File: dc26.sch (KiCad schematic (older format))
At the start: 50 parts, among them J1 CONN_01X10, J2 CONN_01X10, J3 CONN_01X10, Y1 Crystal

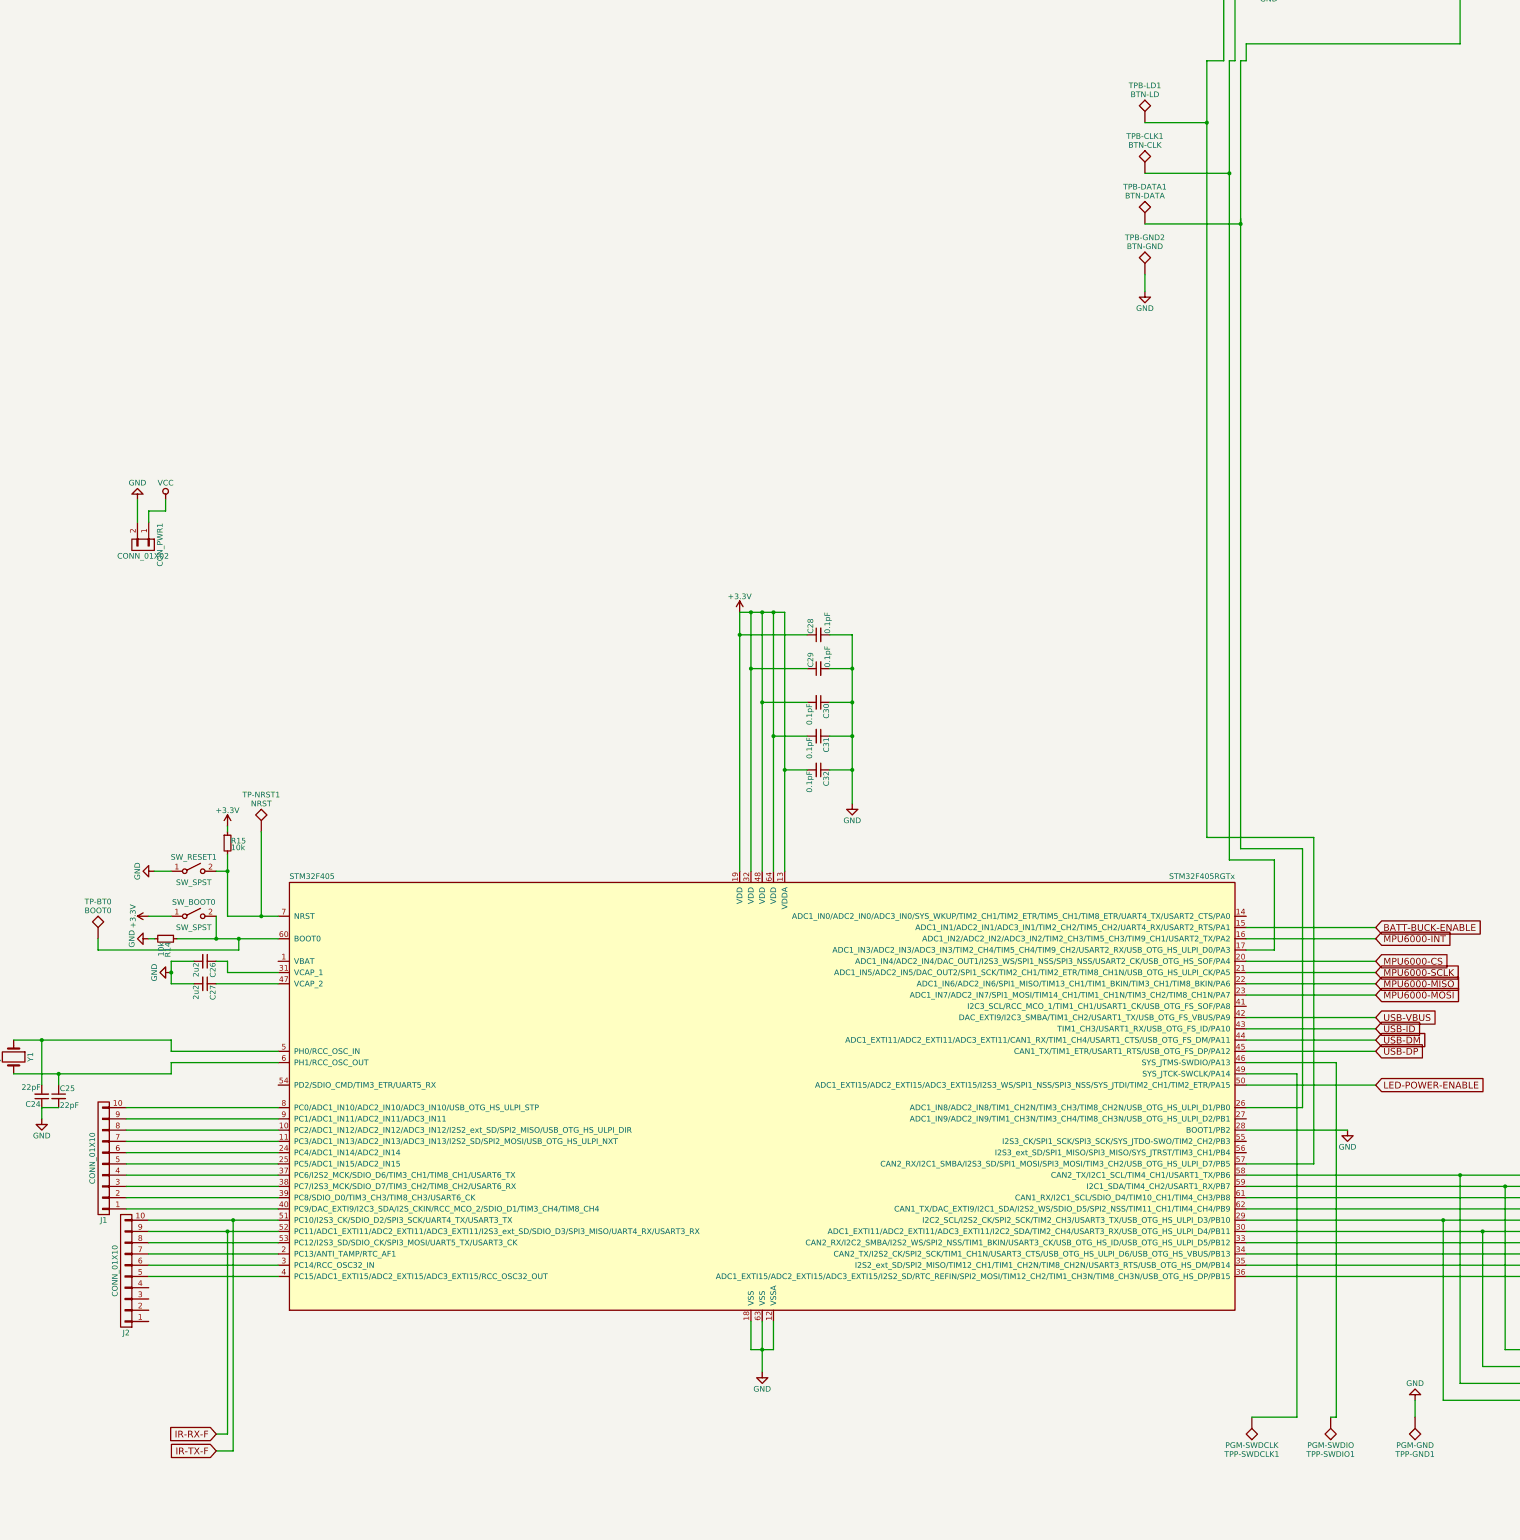
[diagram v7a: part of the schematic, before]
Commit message: Name changes on silk
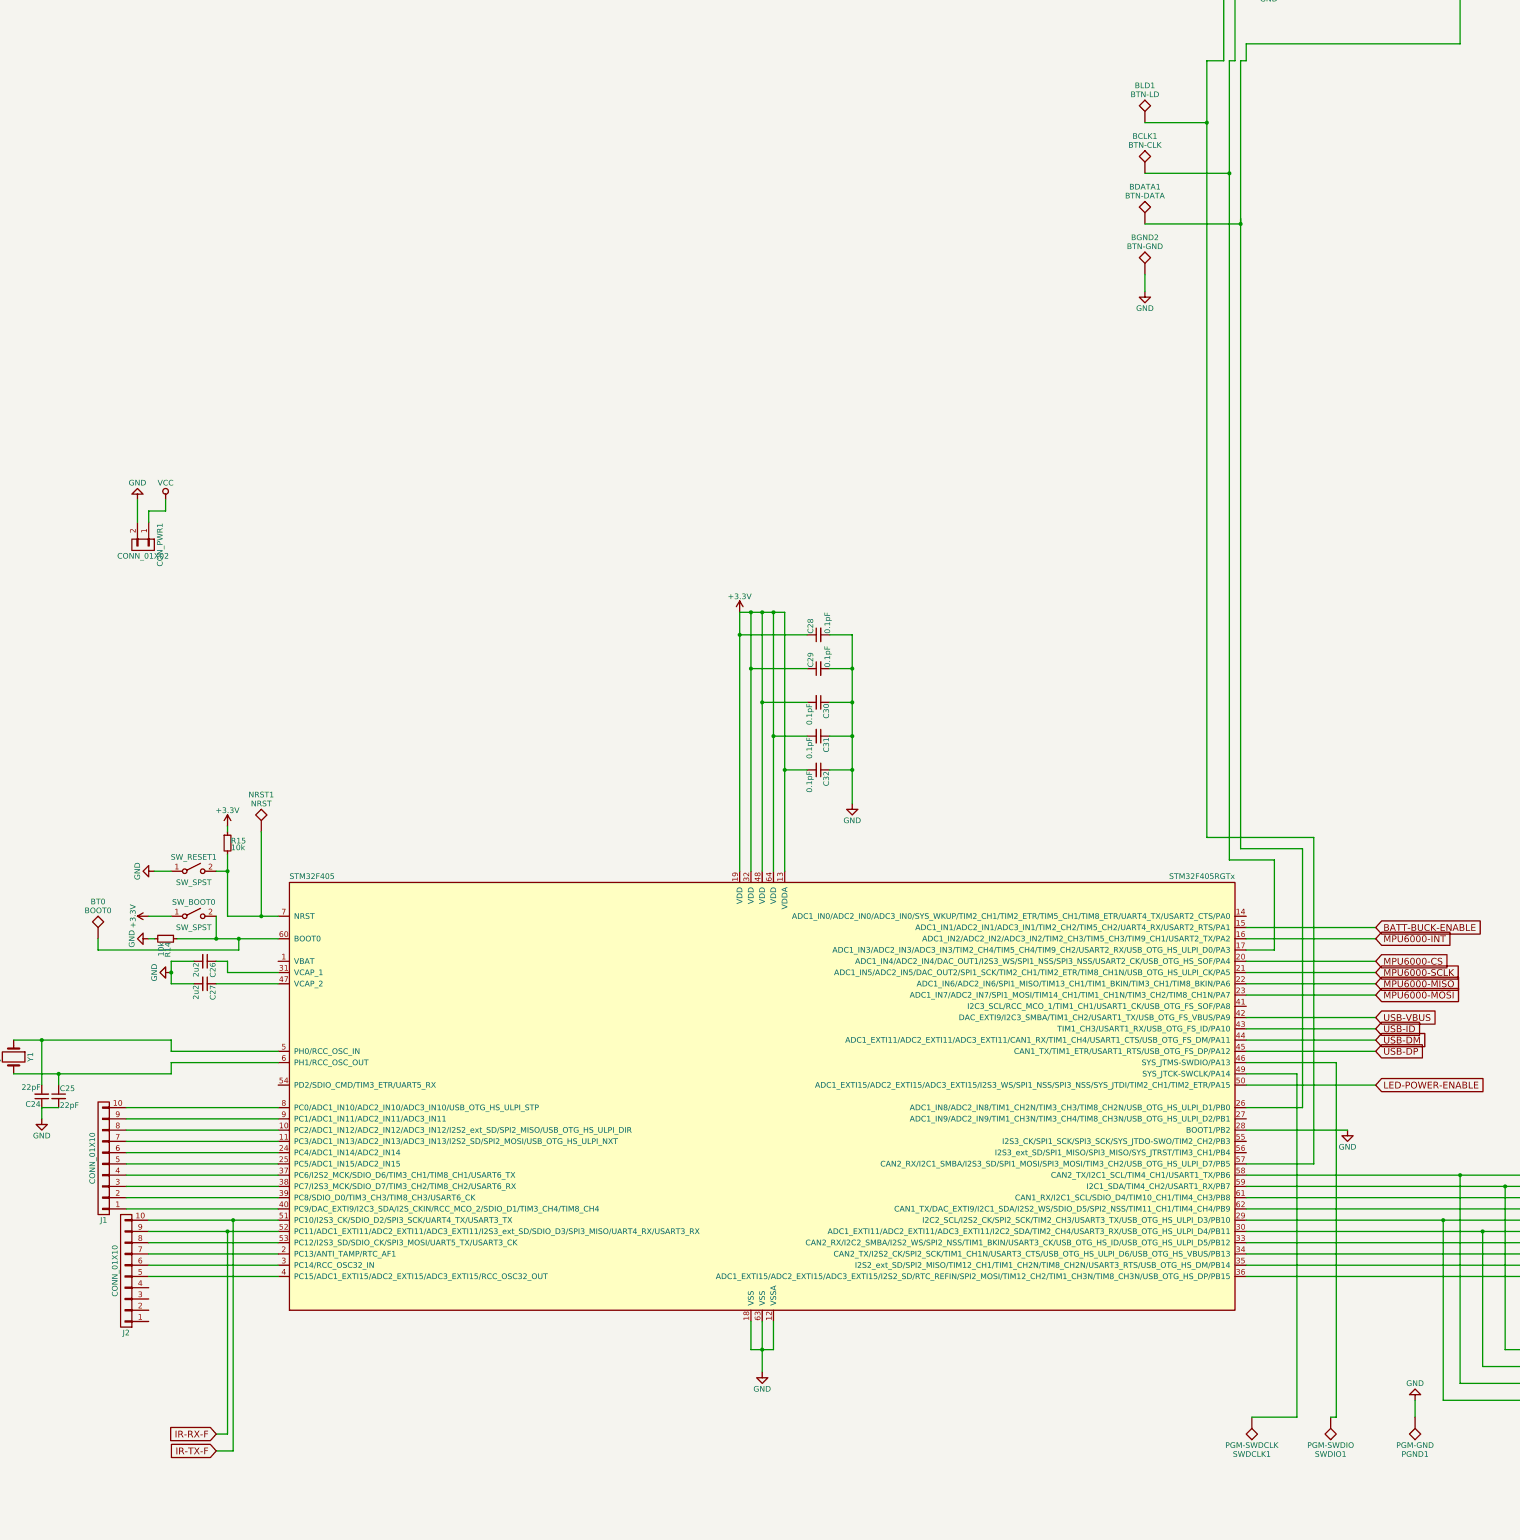
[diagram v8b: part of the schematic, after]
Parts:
- renumbered TPB-CLK1 to BCLK1, TPB-DATA1 to BDATA1, TPB-GND2 to BGND2, TPB-LD1 to BLD1, TP-BT0 to BT0, TP-NRST1 to NRST1, TPP-GND1 to PGND1, TPP-SWDCLK1 to SWDCLK1, TPP-SWDIO1 to SWDIO1
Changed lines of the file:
@@
 $EndComp
 $Comp
-L GND #PWR14
+L GND #PWR01
 U 1 1 5AD27FBE
 P -3450 -6450
-F 0 "#PWR14" H -3450 -6700 50  0001 C CNN
+F 0 "#PWR01" H -3450 -6700 50  0001 C CNN
 F 1 "GND" H -3450 -6600 50  0000 C CNN
 F 2 "" H -3450 -6450 50  0001 C CNN
@@
 $EndComp
 $Comp
-L GND #PWR2
+L GND #PWR02
 U 1 1 5AD5BD83
 P -12550 1050
-F 0 "#PWR2" H -12550 800 50  0001 C CNN
+F 0 "#PWR02" H -12550 800 50  0001 C CNN
 F 1 "GND" H -12550 900 50  0000 C CNN
 F 2 "" H -12550 1050 50  0001 C CNN
@@
 $EndComp
 $Comp
-L VCC #PWR6
+L VCC #PWR03
 U 1 1 5AD5C4E4
 P -12300 1050
-F 0 "#PWR6" H -12300 900 50  0001 C CNN
+F 0 "#PWR03" H -12300 900 50  0001 C CNN
 F 1 "VCC" H -12300 1200 50  0000 C CNN
 F 2 "" H -12300 1050 50  0001 C CNN
@@
 $EndComp
 $Comp
-L GND #PWR15
+L GND #PWR04
 U 1 1 5AD6E593
 P -2500 -5100
-F 0 "#PWR15" H -2500 -5350 50  0001 C CNN
+F 0 "#PWR04" H -2500 -5350 50  0001 C CNN
 F 1 "GND" H -2500 -5250 50  0000 C CNN
 F 2 "" H -2500 -5100 50  0001 C CNN
@@
 $EndComp
 $Comp
-L GND #PWR16
+L GND #PWR05
 U 1 1 5AD6F999
 P -2500 -3550
-F 0 "#PWR16" H -2500 -3800 50  0001 C CNN
+F 0 "#PWR05" H -2500 -3800 50  0001 C CNN
 F 1 "GND" H -2500 -3700 50  0000 C CNN
 F 2 "" H -2500 -3550 50  0001 C CNN
@@
 $EndComp
 $Comp
-L GND #PWR13
+L GND #PWR06
 U 1 1 5AD77A72
 P -3600 -800
-F 0 "#PWR13" H -3600 -1050 50  0001 C CNN
+F 0 "#PWR06" H -3600 -1050 50  0001 C CNN
 F 1 "GND" H -3600 -950 50  0000 C CNN
 F 2 "" H -3600 -800 50  0001 C CNN
@@
 $EndComp
 $Comp
-L GND #PWR10
+L GND #PWR07
 U 1 1 5B04F2A2
 P -7000 8800
-F 0 "#PWR10" H -7000 8550 50  0001 C CNN
+F 0 "#PWR07" H -7000 8550 50  0001 C CNN
 F 1 "GND" H -7000 8650 50  0000 C CNN
 F 2 "" H -7000 8800 50  0001 C CNN
@@
 $EndComp
 $Comp
-L GND #PWR1
+L GND #PWR08
 U 1 1 5B0E23AB
 P -13400 6550
-F 0 "#PWR1" H -13400 6300 50  0001 C CNN
+F 0 "#PWR08" H -13400 6300 50  0001 C CNN
 F 1 "GND" H -13400 6400 50  0000 C CNN
 F 2 "" H -13400 6550 50  0001 C CNN
@@
 $EndComp
 $Comp
-L +3.3V #PWR9
+L +3.3V #PWR09
 U 1 1 5B0D3E01
 P -7200 2050
-F 0 "#PWR9" H -7200 1900 50  0001 C CNN
+F 0 "#PWR09" H -7200 1900 50  0001 C CNN
 F 1 "+3.3V" H -7200 2190 50  0000 C CNN
 F 2 "" H -7200 2050 50  0001 C CNN
@@
 $EndComp
 $Comp
-L GND #PWR7
+L GND #PWR010
 U 1 1 5B0F137D
 P -12250 5250
-F 0 "#PWR7" H -12250 5000 50  0001 C CNN
+F 0 "#PWR010" H -12250 5000 50  0001 C CNN
 F 1 "GND" H -12250 5100 50  0000 C CNN
 F 2 "" H -12250 5250 50  0001 C CNN
@@
 $EndComp
 $Comp
-L GND #PWR11
+L GND #PWR011
 U 1 1 5B0F6A9C
 P -6200 3750
-F 0 "#PWR11" H -6200 3500 50  0001 C CNN
+F 0 "#PWR011" H -6200 3500 50  0001 C CNN
 F 1 "GND" H -6200 3600 50  0000 C CNN
 F 2 "" H -6200 3750 50  0001 C CNN
@@
 $EndComp
 $Comp
-L +3.3V #PWR8
+L +3.3V #PWR012
 U 1 1 5B11C638
 P -11750 3950
-F 0 "#PWR8" H -11750 3800 50  0001 C CNN
+F 0 "#PWR012" H -11750 3800 50  0001 C CNN
 F 1 "+3.3V" H -11750 4090 50  0000 C CNN
 F 2 "" H -11750 3950 50  0001 C CNN
@@
 $EndComp
 $Comp
-L GND #PWR5
+L GND #PWR013
 U 1 1 5B12677B
 P -12400 4350
-F 0 "#PWR5" H -12400 4100 50  0001 C CNN
+F 0 "#PWR013" H -12400 4100 50  0001 C CNN
 F 1 "GND" H -12400 4200 50  0000 C CNN
 F 2 "" H -12400 4350 50  0001 C CNN
@@
 $EndComp
 $Comp
-L GND #PWR4
+L GND #PWR014
 U 1 1 5B1309D3
 P -12450 4950
-F 0 "#PWR4" H -12450 4700 50  0001 C CNN
+F 0 "#PWR014" H -12450 4700 50  0001 C CNN
 F 1 "GND" H -12450 4800 50  0000 C CNN
 F 2 "" H -12450 4950 50  0001 C CNN
@@
 $EndComp
 $Comp
-L +3.3V #PWR3
+L +3.3V #PWR015
 U 1 1 5B136E3C
 P -12450 4750
-F 0 "#PWR3" H -12450 4600 50  0001 C CNN
+F 0 "#PWR015" H -12450 4600 50  0001 C CNN
 F 1 "+3.3V" H -12450 4890 50  0000 C CNN
 F 2 "" H -12450 4750 50  0001 C CNN
@@
 $EndComp
 $Comp
-L GND #PWR17
+L GND #PWR016
 U 1 1 5B13B631
 P -1800 6650
-F 0 "#PWR17" H -1800 6400 50  0001 C CNN
+F 0 "#PWR016" H -1800 6400 50  0001 C CNN
 F 1 "GND" H -1800 6500 50  0000 C CNN
 F 2 "" H -1800 6650 50  0001 C CNN
@@
 $EndComp
 $Comp
-L TEST TPP-SWDCLK1
+L TEST SWDCLK1
 U 1 1 5B1B5199
 P -2650 9200
-F 0 "TPP-SWDCLK1" H -2650 9500 50  0000 C BNN
+F 0 "SWDCLK1" H -2650 9500 50  0000 C BNN
 F 1 "PGM-SWDCLK" H -2650 9450 50  0000 C CNN
 F 2 "Measurement_Points:Measurement_Point_Round-SMD-Pad_Small" H -2650 9200 50  0001 C CNN
@@
 $EndComp
 $Comp
-L TEST TPP-SWDIO1
+L TEST SWDIO1
 U 1 1 5B1B59E8
 P -1950 9200
-F 0 "TPP-SWDIO1" H -1950 9500 50  0000 C BNN
+F 0 "SWDIO1" H -1950 9500 50  0000 C BNN
 F 1 "PGM-SWDIO" H -1950 9450 50  0000 C CNN
 F 2 "Measurement_Points:Measurement_Point_Round-SMD-Pad_Small" H -1950 9200 50  0001 C CNN
@@
 $EndComp
 $Comp
-L TEST TPP-GND1
+L TEST PGND1
 U 1 1 5B1B6C72
 P -1200 9200
-F 0 "TPP-GND1" H -1200 9500 50  0000 C BNN
+F 0 "PGND1" H -1200 9500 50  0000 C BNN
 F 1 "PGM-GND" H -1200 9450 50  0000 C CNN
 F 2 "Measurement_Points:Measurement_Point_Round-SMD-Pad_Small" H -1200 9200 50  0001 C CNN
@@
 $EndComp
 $Comp
-L GND #PWR18
+L GND #PWR017
 U 1 1 5B1B7467
 P -1200 9050
-F 0 "#PWR18" H -1200 8800 50  0001 C CNN
+F 0 "#PWR017" H -1200 8800 50  0001 C CNN
 F 1 "GND" H -1200 8900 50  0000 C CNN
 F 2 "" H -1200 9050 50  0001 C CNN
@@
 $EndComp
 $Comp
-L TEST TP-NRST1
+L TEST NRST1
 U 1 1 5B1CE2A2
 P -11450 4000
-F 0 "TP-NRST1" H -11450 4300 50  0000 C BNN
+F 0 "NRST1" H -11450 4300 50  0000 C BNN
 F 1 "NRST" H -11450 4250 50  0000 C CNN
 F 2 "Measurement_Points:Measurement_Point_Round-SMD-Pad_Small" H -11450 4000 50  0001 C CNN
@@
 $EndComp
 $Comp
-L TEST TP-BT0
+L TEST BT0
 U 1 1 5B1D1428
 P -12900 4950
-F 0 "TP-BT0" H -12900 5250 50  0000 C BNN
+F 0 "BT0" H -12900 5250 50  0000 C BNN
 F 1 "BOOT0" H -12900 5200 50  0000 C CNN
 F 2 "Measurement_Points:Measurement_Point_Round-SMD-Pad_Small" H -12900 4950 50  0001 C CNN
@@
 $EndSheet
 $Comp
-L TEST TPB-LD1
+L TEST BLD1
 U 1 1 5B100C70
 P -3600 -2300
-F 0 "TPB-LD1" H -3600 -2000 50  0000 C BNN
+F 0 "BLD1" H -3600 -2000 50  0000 C BNN
 F 1 "BTN-LD" H -3600 -2050 50  0000 C CNN
 F 2 "Measurement_Points:Measurement_Point_Round-SMD-Pad_Small" H -3600 -2300 50  0001 C CNN
@@
 $EndComp
 $Comp
-L TEST TPB-CLK1
+L TEST BCLK1
 U 1 1 5B101294
 P -3600 -1850
-F 0 "TPB-CLK1" H -3600 -1550 50  0000 C BNN
+F 0 "BCLK1" H -3600 -1550 50  0000 C BNN
 F 1 "BTN-CLK" H -3600 -1600 50  0000 C CNN
 F 2 "Measurement_Points:Measurement_Point_Round-SMD-Pad_Small" H -3600 -1850 50  0001 C CNN
@@
 $EndComp
 $Comp
-L TEST TPB-DATA1
+L TEST BDATA1
 U 1 1 5B101492
 P -3600 -1400
-F 0 "TPB-DATA1" H -3600 -1100 50  0000 C BNN
+F 0 "BDATA1" H -3600 -1100 50  0000 C BNN
 F 1 "BTN-DATA" H -3600 -1150 50  0000 C CNN
 F 2 "Measurement_Points:Measurement_Point_Round-SMD-Pad_Small" H -3600 -1400 50  0001 C CNN
@@
 Connection ~ -3050 -2300
 $Comp
-L TEST TPB-GND2
+L TEST BGND2
 U 1 1 5B105815
 P -3600 -950
-F 0 "TPB-GND2" H -3600 -650 50  0000 C BNN
+F 0 "BGND2" H -3600 -650 50  0000 C BNN
 F 1 "BTN-GND" H -3600 -700 50  0000 C CNN
 F 2 "Measurement_Points:Measurement_Point_Round-SMD-Pad_Small" H -3600 -950 50  0001 C CNN
@@
 Connection ~ -13250 6150
 $Comp
-L +5V #PWR12
+L +5V #PWR018
 U 1 1 5B123F56
 P -5650 -6600
-F 0 "#PWR12" H -5650 -6750 50  0001 C CNN
+F 0 "#PWR018" H -5650 -6750 50  0001 C CNN
 F 1 "+5V" H -5650 -6460 50  0000 C CNN
 F 2 "" H -5650 -6600 50  0001 C CNN
@@
 	-3450 -6550 -3450 -6450
 $Comp
-L GND #PWR22
+L GND #PWR019
 U 1 1 5B188D2F
 P -1100 -5650
-F 0 "#PWR22" H -1100 -5900 50  0001 C CNN
+F 0 "#PWR019" H -1100 -5900 50  0001 C CNN
 F 1 "GND" H -1100 -5800 50  0000 C CNN
 F 2 "" H -1100 -5650 50  0001 C CNN
@@
 	-1100 -5700 -1100 -5650
 $Comp
-L +5V #PWR21
+L +5V #PWR020
 U 1 1 5B1896AE
 P -1100 -5850
-F 0 "#PWR21" H -1100 -6000 50  0001 C CNN
+F 0 "#PWR020" H -1100 -6000 50  0001 C CNN
 F 1 "+5V" H -1100 -5710 50  0000 C CNN
 F 2 "" H -1100 -5850 50  0001 C CNN
@@
 	-1300 -5850 -1100 -5850
 $Comp
-L +5V #PWR19
+L +5V #PWR021
 U 1 1 5B189C3C
 P -1150 -4300
-F 0 "#PWR19" H -1150 -4450 50  0001 C CNN
+F 0 "#PWR021" H -1150 -4450 50  0001 C CNN
 F 1 "+5V" H -1150 -4160 50  0000 C CNN
 F 2 "" H -1150 -4300 50  0001 C CNN
@@
 $EndComp
 $Comp
-L GND #PWR20
+L GND #PWR022
 U 1 1 5B189D37
 P -1150 -4150
-F 0 "#PWR20" H -1150 -4400 50  0001 C CNN
+F 0 "#PWR022" H -1150 -4400 50  0001 C CNN
 F 1 "GND" H -1150 -4300 50  0000 C CNN
 F 2 "" H -1150 -4150 50  0001 C CNN
